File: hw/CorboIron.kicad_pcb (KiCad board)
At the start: 2 copper layers, 62 parts, among them P1 CONN_01X03, P10 CONN_01X04, P11 CONN_01X04, P2 CONN_01X03, P3 CONN_01X03, P4 DIL32, P5 CONN_01X03, P6 CONN_01X04, P7 CONN_01X02, P8 CONN_01X03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

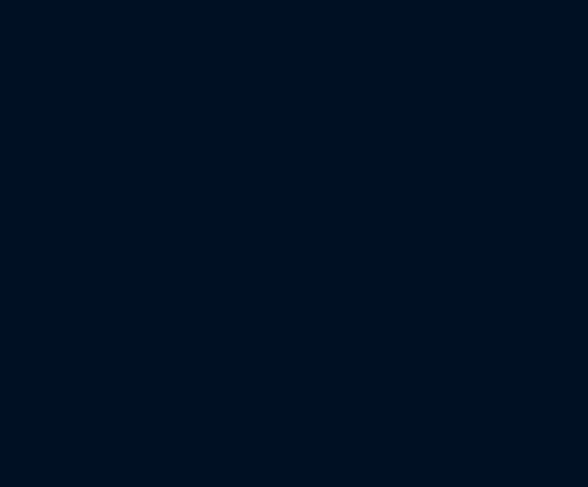
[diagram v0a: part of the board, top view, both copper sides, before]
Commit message: Tried to add footprints
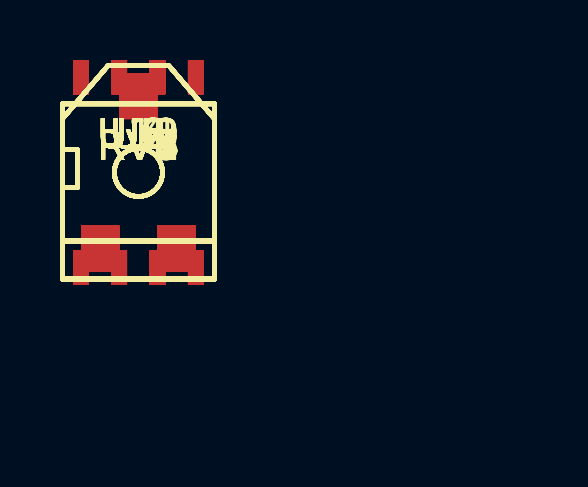
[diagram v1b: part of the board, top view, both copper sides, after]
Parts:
- added RV1, RV2, RV3, RV4, RV5, RV6, RV7, RV8: POT, SMD_Packages:POT_SMD, F.Cu at (0.00, 0.00)
- added U10, U11, U12, U13, U2, U3, U4, U5, U6, U7, U8, U9: LM741, SMD_Packages:SOIC-8-N, F.Cu at (0.00, 0.00)
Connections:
- D1 pad 1: (no net) -> Net-(D1-Pad1)
- D5 pad 1: (no net) -> Net-(D5-Pad1)
- D7 pad 1: (no net) -> Net-(D7-Pad1)
- D9 pad 1: (no net) -> Net-(D9-Pad1)
- P1 pad 2: (no net) -> /TEMP3
- P2 pad 2: (no net) -> /TEMP2
- P3 pad 2: (no net) -> /TEMP1
- P4 pad 16: (no net) -> Net-(P4-Pad16)
- P4 pad 2: (no net) -> +3V3
- P4 pad 3: (no net) -> /REF
- P4 pad 32: (no net) -> Net-(P4-Pad32)
- P5 pad 2: (no net) -> /TEMP0

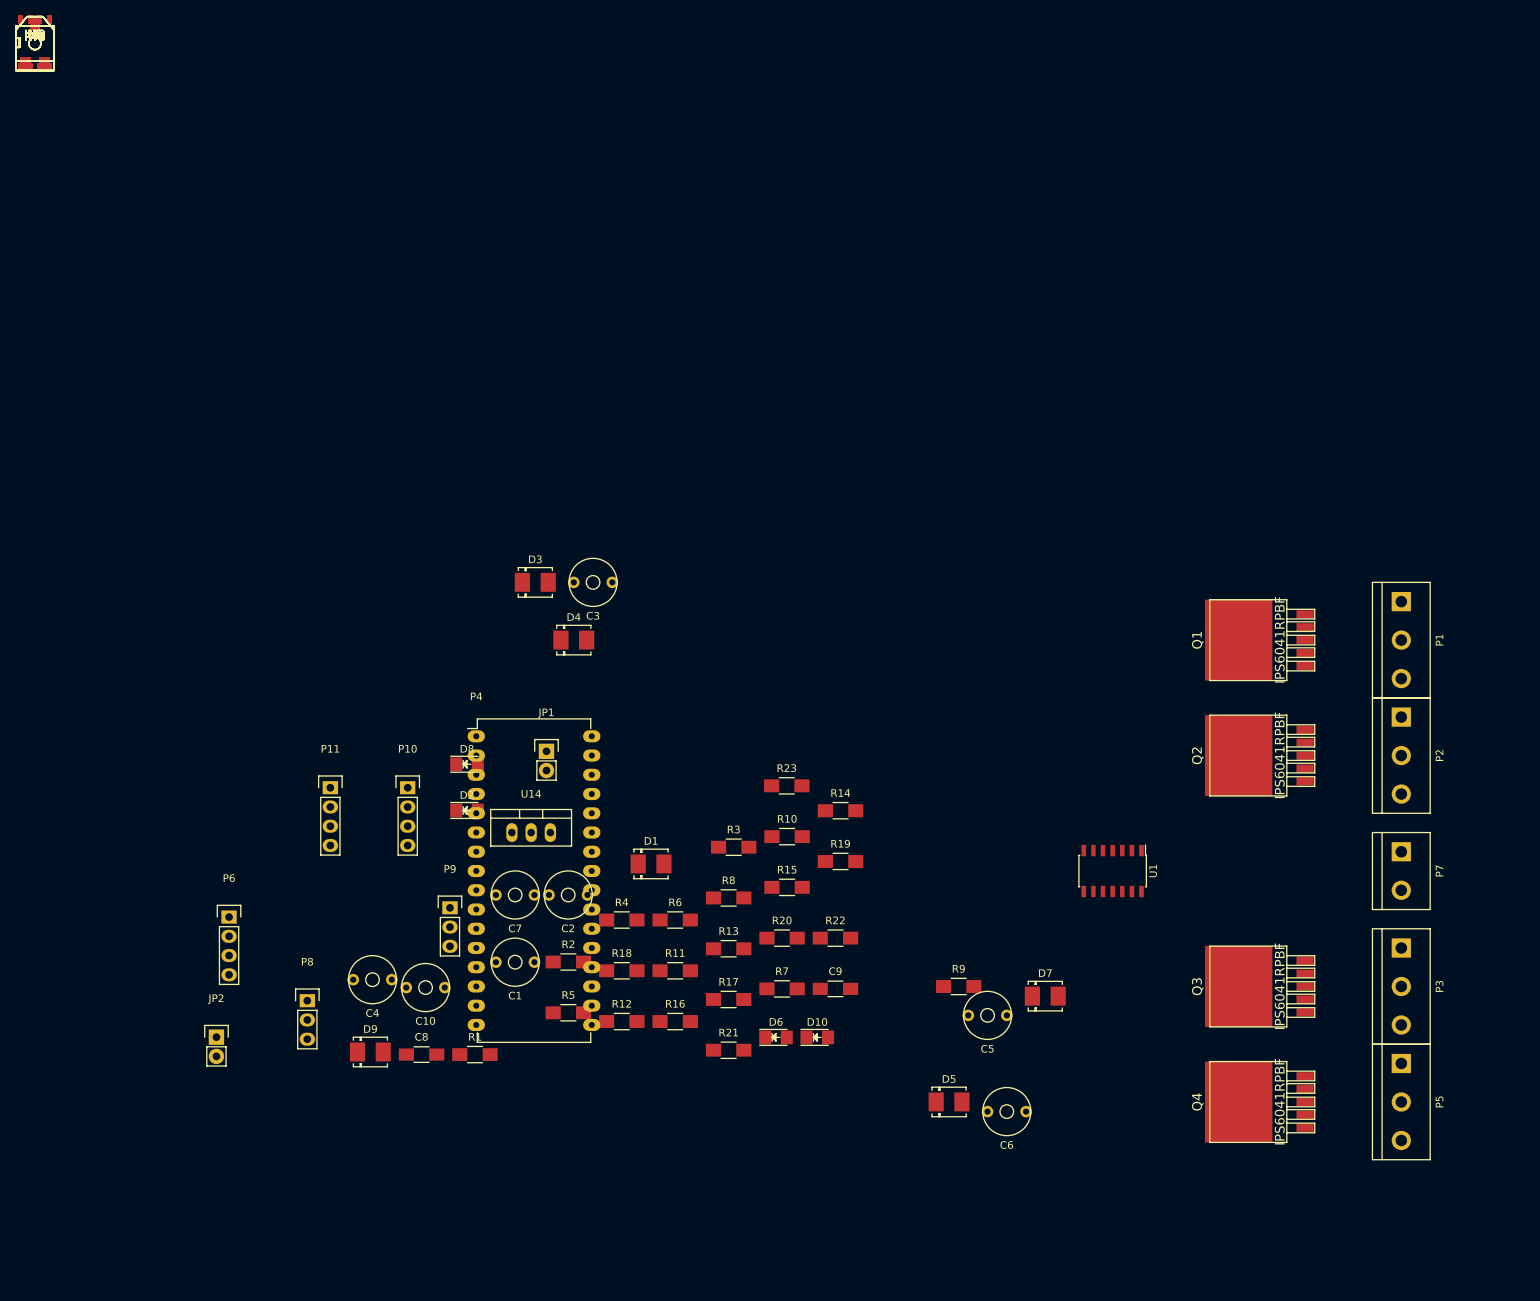
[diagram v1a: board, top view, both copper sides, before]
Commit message: Started placing componets
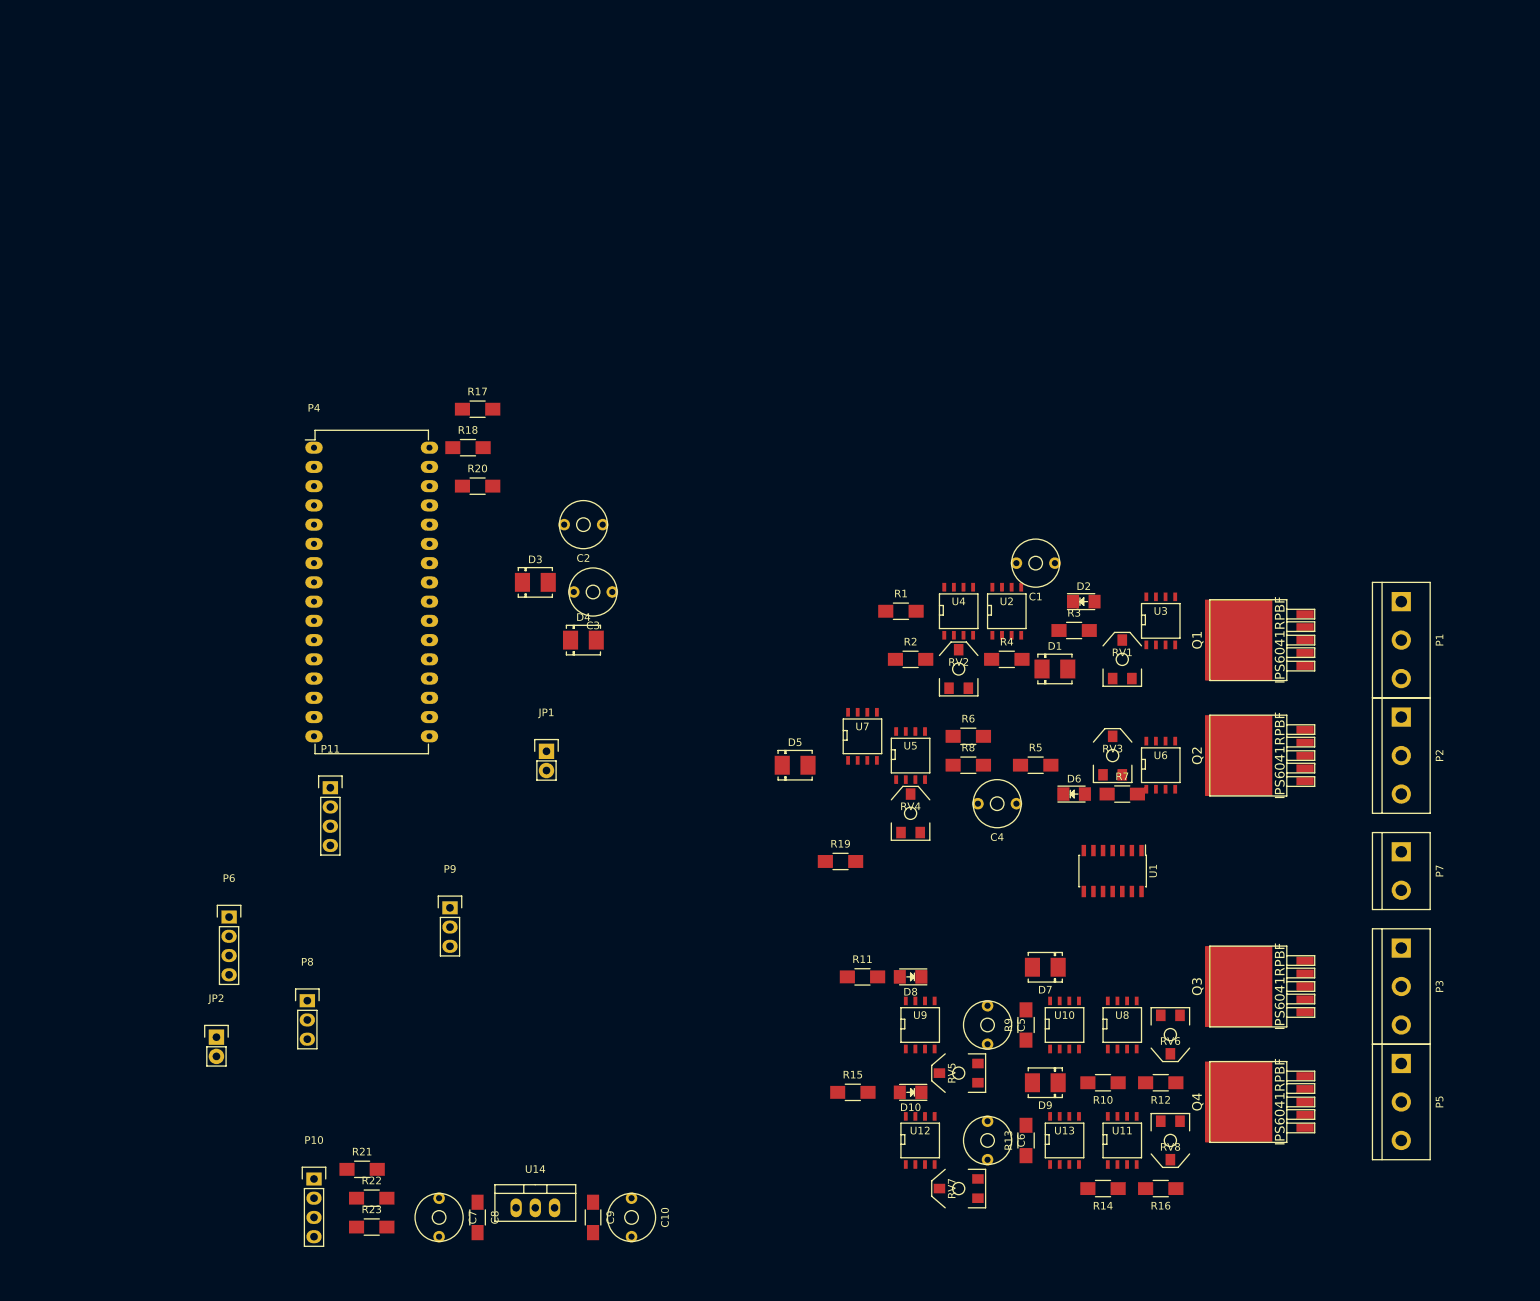
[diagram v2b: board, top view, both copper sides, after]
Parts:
- moved RV8 208.4 mm to (149.9, 144.8), turned to 180 degrees
- moved U11 203.9 mm to (143.5, 144.8)
- moved RV6 198.9 mm to (149.9, 130.8), turned to 180 degrees
- moved U13 198.6 mm to (135.9, 144.8)
- moved RV7 194.2 mm to (121.9, 151.1), turned to 90 degrees
- moved U8 193.3 mm to (143.5, 129.5)
- moved U10 187.7 mm to (135.9, 129.5)
- moved U12 186.0 mm to (116.8, 144.8)
- moved RV5 182.6 mm to (121.9, 135.9), turned to 90 degrees
- moved U6 176.5 mm to (148.6, 95.2)
- moved U9 174.4 mm to (116.8, 129.5)
- moved RV3 170.5 mm to (142.2, 94.0)
- moved U3 167.0 mm to (148.6, 76.2)
- moved RV1 164.9 mm to (143.5, 81.3)
- moved RV4 153.9 mm to (115.6, 101.6)
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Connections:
- P4 pad 16: Net-(P4-Pad16) -> (no net)
- P4 pad 17: Net-(P4-Pad17) -> (no net)
- P4 pad 18: Net-(P4-Pad18) -> /TX1
- P4 pad 19: Net-(P4-Pad19) -> /RX0
- P4 pad 2: +3V3 -> (no net)
- P4 pad 20: /CHARGE_PUMP -> /RST
- P4 pad 21: /PUSH_SW -> GND
- P4 pad 22: /HTR0_EN -> /ROT_A
- P4 pad 23: /HTR1_EN -> /ROT_B
- P4 pad 24: /HTR2_EN -> /HTR3_EN
- P4 pad 25: /HTR3_EN -> /HTR2_EN
- P4 pad 26: /ROT_B -> /HTR1_EN
- P4 pad 27: /ROT_A -> /HTR0_EN
- P4 pad 28: GND -> /PUSH_SW
- P4 pad 29: /RST -> /CHARGE_PUMP
- P4 pad 3: /REF -> (no net)
- P4 pad 30: /RX0 -> Net-(P4-Pad30)
- P4 pad 31: /TX1 -> Net-(P4-Pad31)
- R18 pad 1: Net-(P4-Pad17) -> Net-(P4-Pad32)
- R19 pad 1: Net-(P4-Pad18) -> Net-(P4-Pad31)
- R20 pad 1: Net-(P4-Pad19) -> Net-(P4-Pad30)
- U10 pad 1: Net-(U10-Pad1) -> (no net)
- U10 pad 5: Net-(U10-Pad5) -> (no net)
- U12 pad 1: Net-(U12-Pad1) -> (no net)
- U12 pad 5: Net-(U12-Pad5) -> (no net)
- U13 pad 1: Net-(U13-Pad1) -> (no net)
- U13 pad 5: Net-(U13-Pad5) -> (no net)
- U3 pad 1: Net-(U3-Pad1) -> (no net)
- U3 pad 5: Net-(U3-Pad5) -> (no net)
- U4 pad 1: Net-(U4-Pad1) -> (no net)
- U4 pad 5: Net-(U4-Pad5) -> (no net)
- U6 pad 1: Net-(U6-Pad1) -> (no net)
- U6 pad 5: Net-(U6-Pad5) -> (no net)
- U7 pad 1: Net-(U7-Pad1) -> (no net)
- U7 pad 5: Net-(U7-Pad5) -> (no net)
- U9 pad 1: Net-(U9-Pad1) -> (no net)
- U9 pad 5: Net-(U9-Pad5) -> (no net)

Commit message: Horror!
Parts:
- P4: value DIL32 -> Arduino_nano
- moved JP2 151.6 mm to (175.0, 117.9), turned to 270 degrees
- moved P6 141.4 mm to (166.4, 129.3), turned to 270 degrees
- moved P11 136.7 mm to (175.3, 109.2), turned to 90 degrees
- moved D3 132.9 mm to (187.5, 125.2), turned to 270 degrees
- moved C10 123.8 mm to (190.5, 101.6)
- moved C8 123.8 mm to (170.2, 101.6)
- moved C7 123.8 mm to (165.1, 101.6)
- moved C9 123.8 mm to (185.4, 101.6)
- moved U14 123.8 mm to (177.8, 100.3)
- moved C3 118.7 mm to (180.3, 124.5), turned to 90 degrees
- moved P4 115.3 mm to (129.5, 121.9), turned to 90 degrees
- moved JP1 113.5 mm to (180.3, 105.4), turned to 90 degrees
- moved D4 110.3 mm to (172.7, 124.5), turned to 270 degrees
- moved C2 104.6 mm to (152.4, 130.8), turned to 180 degrees
- moved R17 101.1 mm to (131.6, 118.1)
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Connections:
- C4 pad 1: /TEMP0_MIN -> /TEMP2_MIN
- D5 pad 2: /TEMP0_MIN -> /TEMP2_MIN
- P4 pad 13: /RST -> (no net)
- P4 pad 20: /RST -> (no net)
- R5 pad 1: /TEMP0_MIN -> /TEMP2_MIN
- RV2 pad 2: Net-(RV2-Pad2) -> /V_NEG
- RV4 pad 2: Net-(RV4-Pad2) -> /V_NEG
- RV6 pad 2: Net-(RV6-Pad2) -> /V_NEG
- U14 pad 1: (no net) -> +12V
- U14 pad 2: (no net) -> GND
- U14 pad 3: (no net) -> +5V
- U2 pad 4: Net-(RV2-Pad2) -> /V_NEG
- U5 pad 4: Net-(RV4-Pad2) -> /V_NEG
- U6 pad 2: /TEMP0_MIN -> /TEMP2_MIN
- U7 pad 2: /TEMP0_MIN -> /TEMP2_MIN
- U8 pad 4: Net-(RV6-Pad2) -> /V_NEG
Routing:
- net GND: track 0.00 -> 490.2 mm, vias 0 -> 17
- net +12V: track 0.00 -> 397.8 mm, vias 0 -> 21
- net /V_NEG: track 0.00 -> 286.2 mm, vias 0 -> 16
- net +5V: track 0.00 -> 253.2 mm, vias 0 -> 2
- net /HTR0_CTL': track 0.00 -> 100.7 mm, vias 0 -> 4
- net /TEMP3_OK: track 0.00 -> 97.1 mm, vias 0 -> 5
- net /TEMP0_AMP: track 0.00 -> 94.9 mm, vias 0 -> 1
- net /TEMP2_OK: track 0.00 -> 64.2 mm, vias 0 -> 3
- net /TEMP0_OK: track 0.00 -> 63.7 mm, vias 0 -> 4
- net /TEMP3: track 0.00 -> 63.3 mm
- net /HTR1_CTL: track 0.00 -> 62.2 mm, vias 0 -> 4
- net /HTR3_CTL: track 0.00 -> 56.6 mm, vias 0 -> 2
- net /TEMP0: track 0.00 -> 54.4 mm
- net /TEMP1: track 0.00 -> 54.3 mm
- net /TEMP2: track 0.00 -> 49.1 mm
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- added copper zone on B.Cu, net +12V
- added copper zone on B.Cu, net GND
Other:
- board outline added: 158.8 x 99.1 mm
- net class High Power added: clearance 0.2, trace_width 2, via_dia 2, via_drill 1
- net class Minimum added: clearance 0.1524, trace_width 0.1524, via_dia 0.508, via_drill 0.3302
- net class Normal added: clearance 0.2, trace_width 0.5, via_dia 0.6, via_drill 0.35
- rule trace_min: 0.2 -> 0.1524
- rule via_min_drill: 0.3 -> 0.3302
- rule via_min_size: 0.4 -> 0.508

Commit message: Started pretty version
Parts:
- removed RV2, RV4, RV6, RV8: POT, SMD_Packages:POT_SMD
- removed U10, U11, U12, U13, U5, U6, U7, U8, U9: LM741, SMD_Packages:SOIC-8-N
- added D11: D, Diodes_SMD:SOD-123, F.Cu at (160.0, 67.8)
- added D12: D, Diodes_SMD:SOD-123, F.Cu at (164.8, 95.8)
- added D13: D, Diodes_SMD:SOD-123, F.Cu at (146.7, 146.4)
- added D14: D, Diodes_SMD:SOD-123, F.Cu at (148.0, 159.9)
- added R24: R, Resistors_SMD:R_0805, F.Cu at (145.3, 71.1)
- added R25: R, Resistors_SMD:R_0805, F.Cu at (160.3, 91.9)
- added R26: R, Resistors_SMD:R_0805, F.Cu at (161.5, 72.6)
- added R27: R, Resistors_SMD:R_0805, F.Cu at (156.2, 72.1)
- added R28: R, Resistors_SMD:R_0805, F.Cu at (146.3, 76.5)
- added R29: R, Resistors_SMD:R_0805, F.Cu at (136.9, 70.1)
- added R30: R, Resistors_SMD:R_0805, F.Cu at (141.5, 100.3)
- added R31: R, Resistors_SMD:R_0805, F.Cu at (158.5, 94.7)
- added R32: R, Resistors_SMD:R_0805, F.Cu at (125.5, 94.2)
- added R33: R, Resistors_SMD:R_0805, F.Cu at (156.2, 88.6)
- added R34: R, Resistors_SMD:R_0805, F.Cu at (145.3, 97.5)
- added R35: R, Resistors_SMD:R_0805, F.Cu at (132.6, 95.5)
- added R36: R, Resistors_SMD:R_0805, F.Cu at (153.2, 138.4)
- added R37: R, Resistors_SMD:R_0805, F.Cu at (150.9, 146.6)
- added R38: R, Resistors_SMD:R_0805, F.Cu at (149.6, 138.4)
- added R39: R, Resistors_SMD:R_0805, F.Cu at (153.2, 143.5)
- added R40: R, Resistors_SMD:R_0805, F.Cu at (149.9, 144.0)
- added R41: R, Resistors_SMD:R_0805, F.Cu at (146.1, 144.0)
- added R42: R, Resistors_SMD:R_0805, F.Cu at (154.7, 152.1)
- added R43: R, Resistors_SMD:R_0805, F.Cu at (152.5, 159.9)
- added R44: R, Resistors_SMD:R_0805, F.Cu at (150.9, 152.1)
- added R45: R, Resistors_SMD:R_0805, F.Cu at (154.2, 157.0)
- added R46: R, Resistors_SMD:R_0805, F.Cu at (150.9, 157.7)
- added R47: R, Resistors_SMD:R_0805, F.Cu at (147.3, 157.2)
- D1, D3, D4, D5, D7, D9: footprint Diodes_SMD:DO-214BA -> Diodes_SMD:SOD-123
- R1, R10, R11, R12, R13, R14, R15, R16, R17, R18, R19, R2, R20, R21, R22, R23, R3, R4, R5, R6, R7, R8, R9: footprint Resistors_SMD:R_1206_HandSoldering -> Resistors_SMD:R_0805
- U1: value 74LS08 -> LM324; footprint Housings_SOIC:SOIC-14_3.9x8.7mm_Pitch1.27mm -> SMD_Packages:SO14N
- U2, U3, U4: value LM741 -> LM324; footprint SMD_Packages:SOIC-8-N -> SMD_Packages:SO14N
- moved U4 80.1 mm to (140.8, 156.1), turned to 90 degrees
- moved U3 67.6 mm to (139.6, 142.6), turned to 90 degrees
- moved U1 42.0 mm to (153.9, 72.4)
- moved C2 32.7 mm to (180.6, 114.3)
- moved D7 17.5 mm to (133.9, 145.4), turned to 90 degrees
- moved U2 17.5 mm to (151.1, 93.5)
- moved D9 15.2 mm to (135.0, 158.6), turned to 90 degrees
- moved R12 13.6 mm to (146.1, 141.2)
- moved R16 12.6 mm to (147.3, 154.7)
- moved R11 12.3 mm to (122.9, 139.2), turned to 0 degrees
- moved RV5 10.8 mm to (122.4, 144.3), turned to 0 degrees
- moved C5 9.73 mm to (128.5, 144.8), turned to 0 degrees
- moved RV7 9.67 mm to (122.7, 157.7), turned to 0 degrees
- moved R10 9.16 mm to (146.1, 138.4)
- moved R14 8.75 mm to (147.3, 152.1)
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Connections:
- Q1 pad 2: /HTR3_CTL -> Net-(Q1-Pad2)
- Q2 pad 2: /HTR2_CTL -> Net-(Q2-Pad2)
- Q3 pad 2: /HTR1_CTL -> Net-(Q3-Pad2)
- Q4 pad 2: /HTR0_CTL' -> Net-(Q4-Pad2)
- U1 pad 1: /HTR3_EN -> /HTR3_CTL
- U1 pad 10: /TEMP1_OK -> Net-(RV1-Pad2)
- U1 pad 11: /HTR0_CTL' -> /V_NEG
- U1 pad 12: /HTR0_EN -> /TEMP3_AMP
- U1 pad 13: /TEMP0_OK -> /TEMP3_MIN
- U1 pad 14: +5V -> Net-(D1-Pad1)
- U1 pad 2: /TEMP3_OK -> Net-(R28-Pad1)
- U1 pad 3: /HTR3_CTL -> Net-(R24-Pad1)
- U1 pad 4: /HTR2_EN -> +12V
- U1 pad 5: /TEMP2_OK -> /TEMP3
- U1 pad 6: /HTR2_CTL -> Net-(R2-Pad1)
- U1 pad 7: GND -> /TEMP3_AMP
- U1 pad 8: /HTR1_CTL -> /TEMP3_OK
- U1 pad 9: /HTR1_EN -> /TEMP3_MIN
- U2 pad 1: Net-(RV2-Pad3) -> /HTR2_CTL
- U2 pad 2: Net-(R2-Pad1) -> Net-(R34-Pad1)
- U2 pad 3: /TEMP3 -> Net-(R30-Pad1)
- U2 pad 4: /V_NEG -> +12V
- U2 pad 5: Net-(RV2-Pad1) -> /TEMP2
- U2 pad 6: /TEMP3_AMP -> Net-(R6-Pad1)
- U2 pad 7: +12V -> /TEMP2_AMP
- U2 pad 8: (no net) -> /TEMP2_OK
- U3 pad 1: (no net) -> /HTR1_CTL
- U3 pad 2: /TEMP3_MIN -> Net-(R40-Pad1)
- U3 pad 3: Net-(RV1-Pad2) -> Net-(R36-Pad1)
- U3 pad 4: /V_NEG -> +12V
- U3 pad 5: (no net) -> /TEMP1
- U3 pad 6: /TEMP3_OK -> Net-(R10-Pad1)
- U3 pad 7: +12V -> /TEMP1_AMP
- U3 pad 8: (no net) -> /TEMP1_OK
- U4 pad 1: (no net) -> /HTR0_CTL'
- U4 pad 2: /TEMP3_MIN -> Net-(R46-Pad1)
- U4 pad 3: /TEMP3_AMP -> Net-(R42-Pad1)
- U4 pad 4: /V_NEG -> +12V
- U4 pad 5: (no net) -> /TEMP0
- U4 pad 6: Net-(D1-Pad1) -> Net-(R14-Pad1)
- U4 pad 7: +12V -> /TEMP0_AMP
- U4 pad 8: (no net) -> /TEMP0_OK
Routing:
- net GND: track 490.2 -> 6.95 mm, vias 17 -> 0
- net +12V: track 397.8 -> 0.00 mm, vias 21 -> 0
- net /V_NEG: track 286.2 -> 0.00 mm, vias 16 -> 0
- net +5V: track 253.2 -> 0.00 mm, vias 2 -> 0
- net /HTR0_CTL': track 100.7 -> 2.17 mm, vias 4 -> 0
- net /TEMP3_OK: track 97.1 -> 0.00 mm, vias 5 -> 0
- net /TEMP0_AMP: track 94.9 -> 2.28 mm, vias 1 -> 0
- net /TEMP2_OK: track 64.2 -> 0.00 mm, vias 3 -> 0
- net /TEMP3: track 63.3 -> 0.00 mm
- net /HTR1_CTL: track 62.2 -> 0.00 mm, vias 4 -> 0
- net /HTR3_CTL: track 56.6 -> 0.00 mm, vias 2 -> 0
- net /TEMP0: track 54.4 -> 0.00 mm
- net /TEMP1: track 54.3 -> 0.00 mm
- net /TEMP2: track 49.1 -> 0.00 mm
- net /TEMP1_OK: track 49.1 -> 0.00 mm, vias 5 -> 0
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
